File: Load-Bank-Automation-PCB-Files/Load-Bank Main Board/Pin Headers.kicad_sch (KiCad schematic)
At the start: 20 parts, among them J10 Conn_02x03_Counter_Clockwise, J11 Conn_02x03_Counter_Clockwise, J12 Conn_02x03_Counter_Clockwise, J13 Conn_02x03_Counter_Clockwise, J14 Conn_02x03_Counter_Clockwise, J15 Conn_02x03_Counter_Clockwise, J16 Conn_02x03_Counter_Clockwise, J17 Conn_02x03_Counter_Clockwise, J18 Conn_02x03_Counter_Clockwise, J19 Conn_02x03_Counter_Clockwise, J20 Conn_02x03_Counter_Clockwise, J21 Conn_02x03_Counter_Clockwise, J22 Conn_02x03_Counter_Clockwise, J23 Conn_02x03_Counter_Clockwise, J4 Conn_02x03_Counter_Clockwise, J5 Conn_02x03_Counter_Clockwise, J6 Conn_02x03_Counter_Clockwise, J7 Conn_02x03_Counter_Clockwise, J8 Conn_02x03_Counter_Clockwise, J9 Conn_02x03_Counter_Clockwise

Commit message: Schematic for review
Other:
- note added: "- These pins will conenct the MOSFET Boards to the MCU"
- note added: "Notes"
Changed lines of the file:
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@@
 	(paper "A4")
+	(rectangle
+		(start 195.834 65.278)
+		(end 255.524 71.628)
+		(stroke
+			(width 0.2032)
+			(type dash)
+		)
+		(fill
+			(type none)
+		)
+	)
 	(rectangle
 		(start 43.18 15.24)
@@
 		)
 	)
+	(text "- These pins will conenct the MOSFET Boards to the MCU"
+		(exclude_from_sim no)
+		(at 196.85 68.58 0)
+		(effects
+			(font
+				(size 1.27 1.27)
+				(thickness 0.1588)
+			)
+			(justify left)
+		)
+	)
+	(text "Notes"
+		(exclude_from_sim no)
+		(at 195.58 62.992 0)
+		(effects
+			(font
+				(size 1.778 1.778)
+				(thickness 0.3556)
+				(bold yes)
+			)
+			(justify left)
+		)
+	)

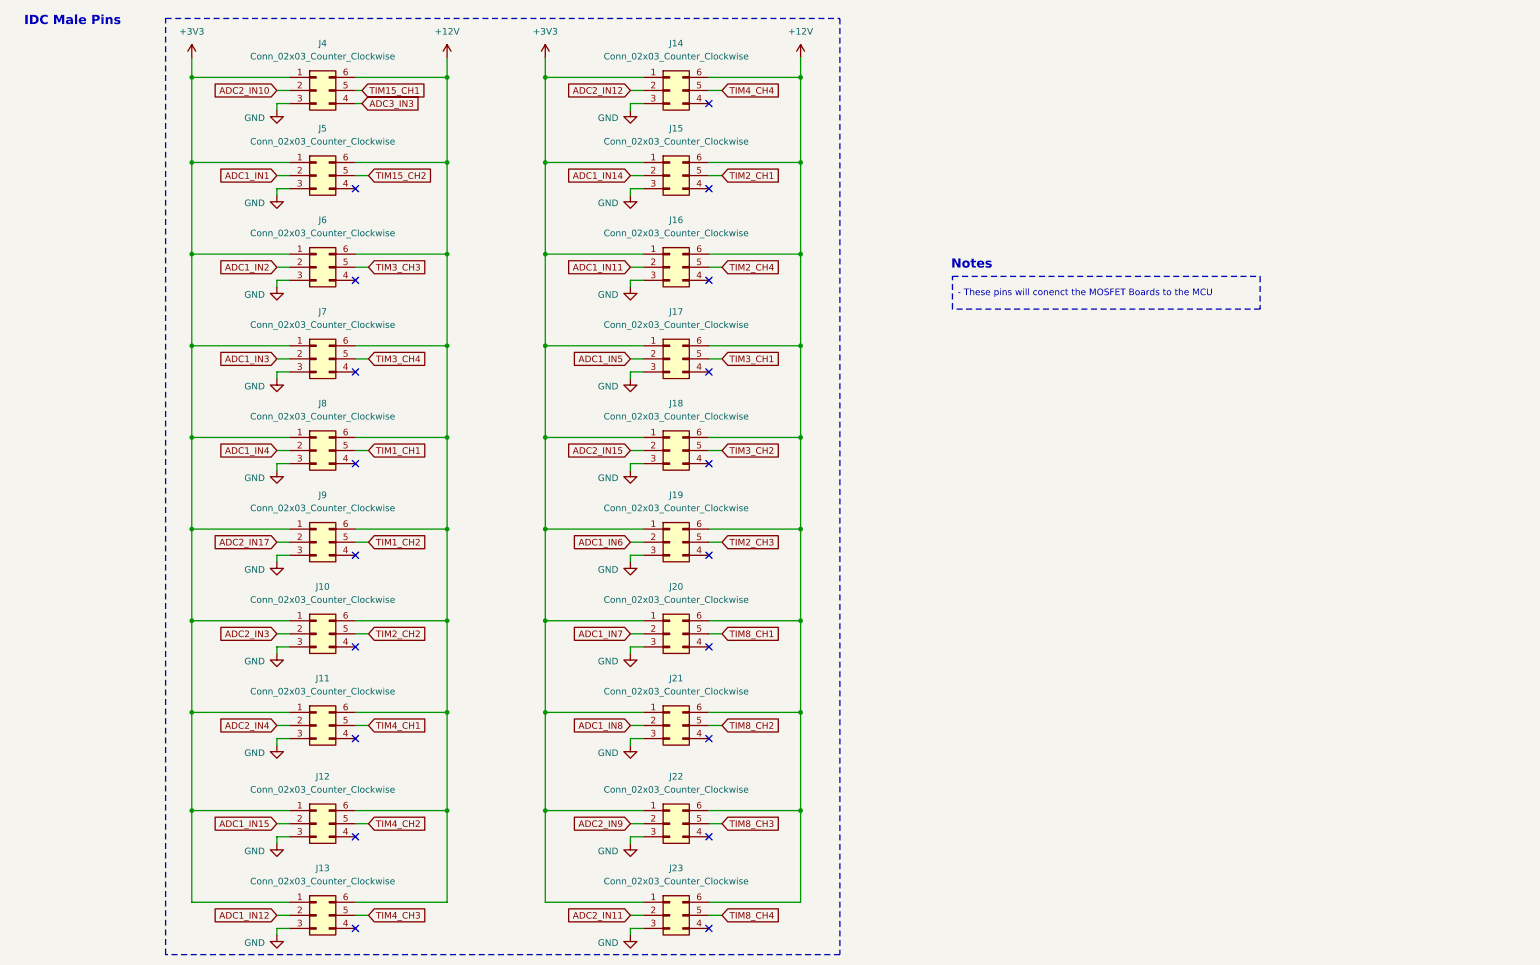
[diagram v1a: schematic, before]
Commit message: All footprints assigned and new schematic changes
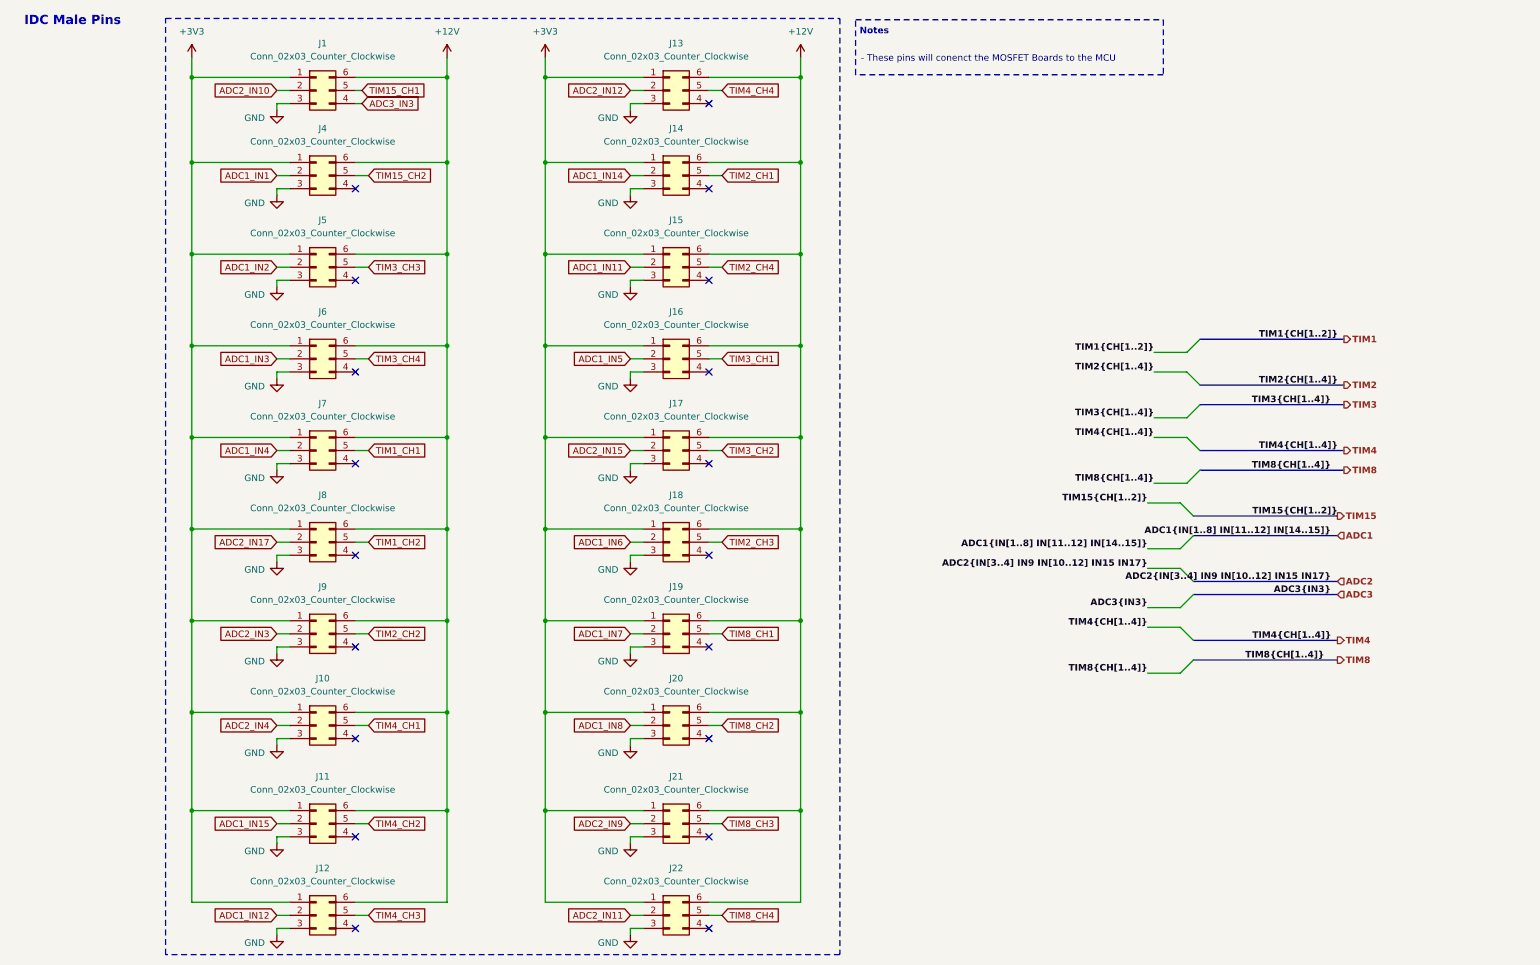
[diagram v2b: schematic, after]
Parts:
- renumbered J4 to J1, J11 to J10, J12 to J11, J13 to J12, J14 to J13, J15 to J14, J16 to J15, J17 to J16, J18 to J17, J19 to J18, J20 to J19, J21 to J20, J22 to J21, J23 to J22, J5 to J4, J6 to J5, J7 to J6, J8 to J7, J9 to J8, J10 to J9

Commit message: Clearing up electrical rule errors
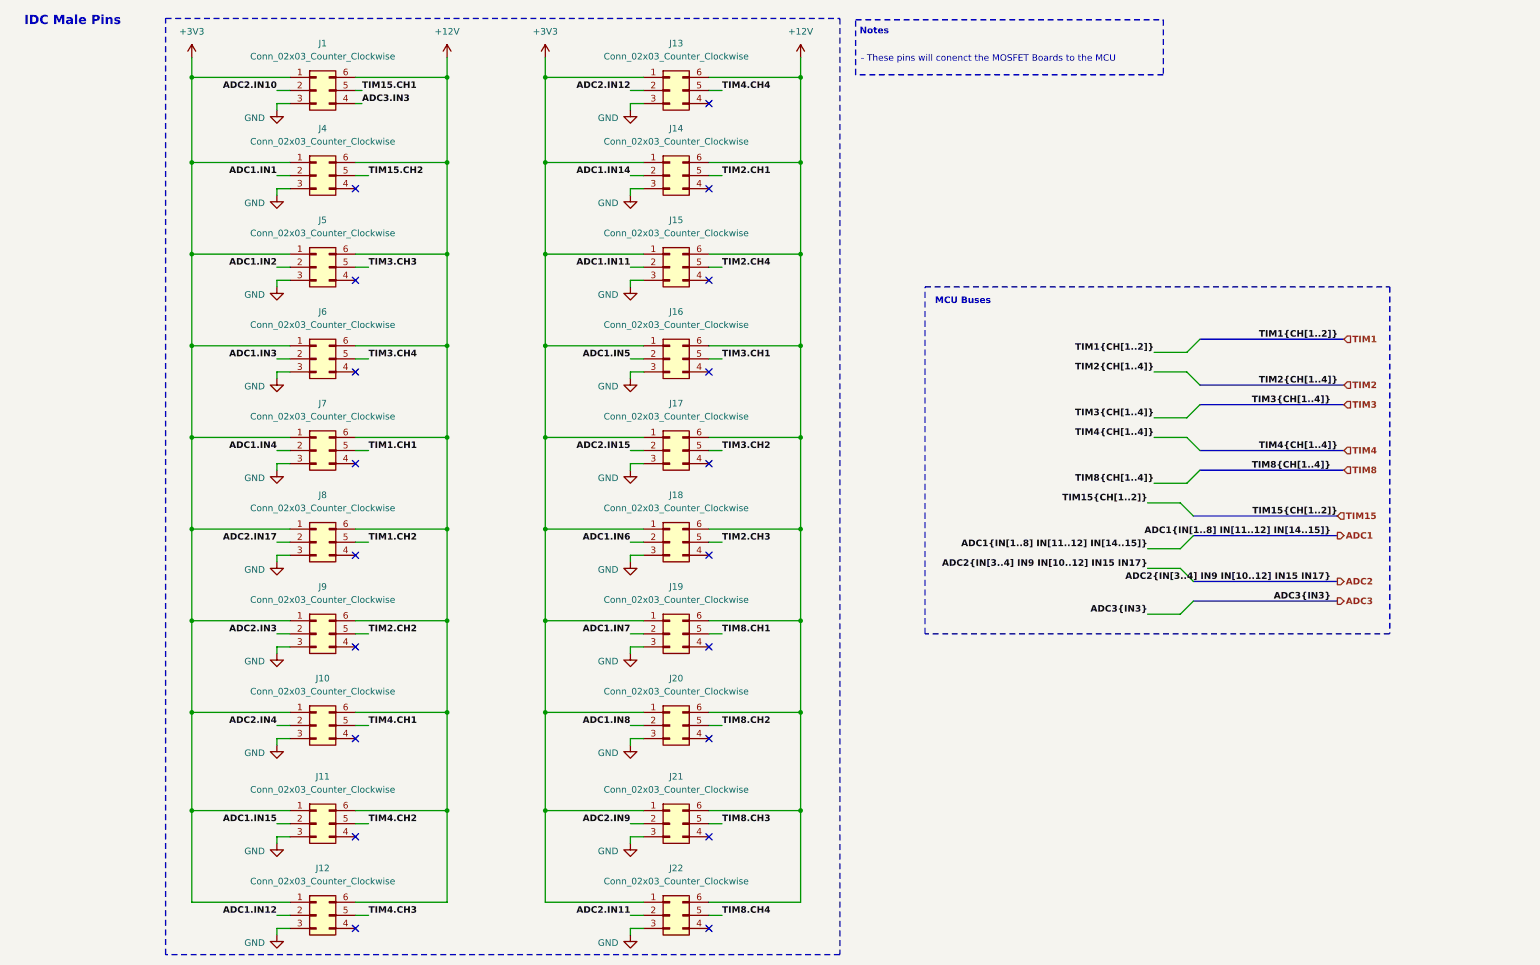
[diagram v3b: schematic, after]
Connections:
- net ADC1_IN1 renamed ADC1.IN1
- net ADC1_IN11 renamed ADC1.IN11
- net ADC1_IN12 renamed ADC1.IN12
- net ADC1_IN14 renamed ADC1.IN14
- net ADC1_IN15 renamed ADC1.IN15
- net ADC1_IN2 renamed ADC1.IN2
- net ADC1_IN3 renamed ADC1.IN3
- net ADC1_IN4 renamed ADC1.IN4
- net ADC1_IN5 renamed ADC1.IN5
- net ADC1_IN6 renamed ADC1.IN6
- net ADC1_IN7 renamed ADC1.IN7
- net ADC1_IN8 renamed ADC1.IN8
- net ADC2_IN10 renamed ADC2.IN10
- net ADC2_IN11 renamed ADC2.IN11
- net ADC2_IN12 renamed ADC2.IN12
- net ADC2_IN15 renamed ADC2.IN15
- net ADC2_IN17 renamed ADC2.IN17
- net ADC2_IN3 renamed ADC2.IN3
- net ADC2_IN4 renamed ADC2.IN4
- net ADC2_IN9 renamed ADC2.IN9
- net ADC3_IN3 renamed ADC3.IN3
- net TIM15_CH1 renamed TIM15.CH1
- net TIM15_CH2 renamed TIM15.CH2
- net TIM1_CH1 renamed TIM1.CH1
- net TIM1_CH2 renamed TIM1.CH2
- net TIM2_CH1 renamed TIM2.CH1
- net TIM2_CH2 renamed TIM2.CH2
- net TIM2_CH3 renamed TIM2.CH3
- net TIM2_CH4 renamed TIM2.CH4
- net TIM3_CH1 renamed TIM3.CH1
- net TIM3_CH2 renamed TIM3.CH2
- net TIM3_CH3 renamed TIM3.CH3
- net TIM3_CH4 renamed TIM3.CH4
- net TIM4_CH1 renamed TIM4.CH1
- net TIM4_CH2 renamed TIM4.CH2
- net TIM4_CH3 renamed TIM4.CH3
- net TIM4_CH4 renamed TIM4.CH4
- net TIM8_CH1 renamed TIM8.CH1
- net TIM8_CH2 renamed TIM8.CH2
- net TIM8_CH3 renamed TIM8.CH3
- net TIM8_CH4 renamed TIM8.CH4
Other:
- note added: "MCU Buses"

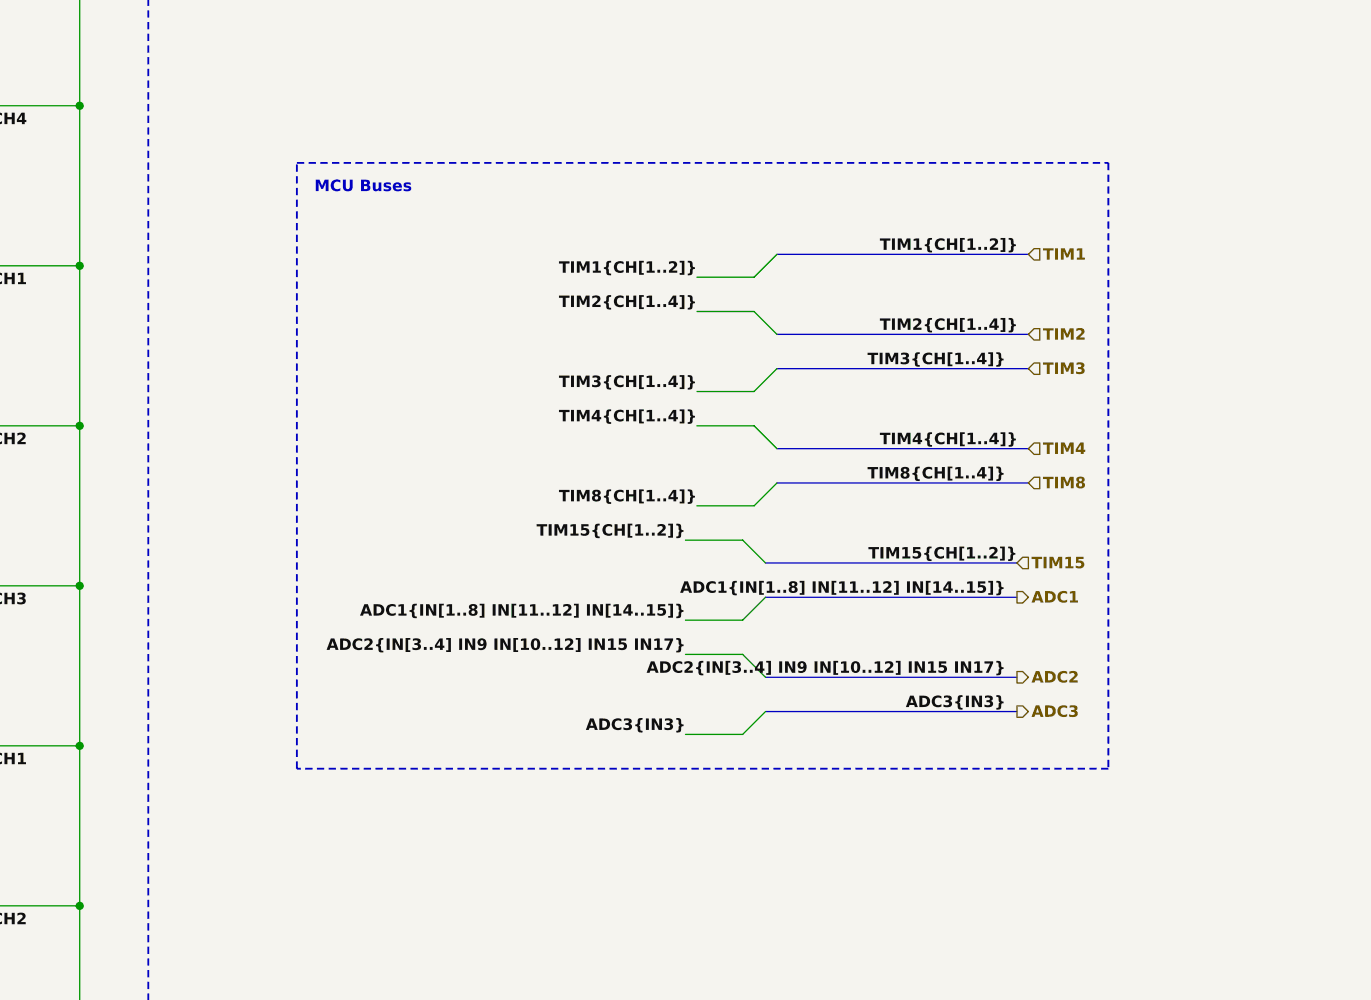
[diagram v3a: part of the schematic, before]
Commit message: Schematic complete and  ready for review
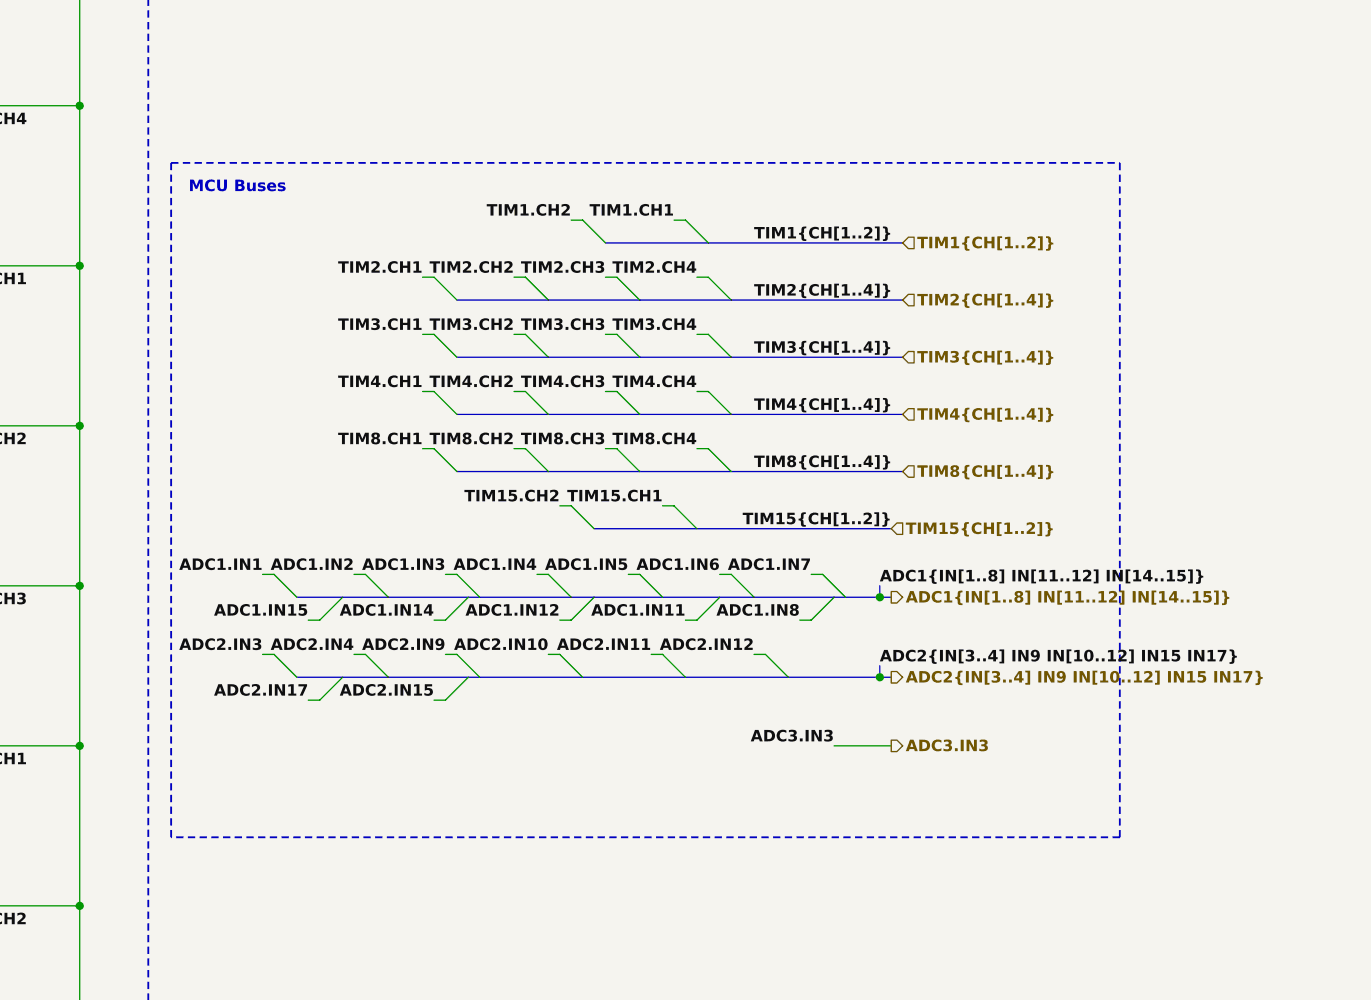
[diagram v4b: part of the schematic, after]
